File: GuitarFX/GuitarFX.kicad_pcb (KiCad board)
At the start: 4 copper layers, 70 x 85 mm, 122 parts, among them IC401 PCM3060PWR, J202 Screw_Terminal_01x02, J301 USB_C_Receptacle_USB2.0, J302 Conn_ARM_SWD_TagConnect_TC2030, J303 Screw_Terminal_01x06, J401 Screw_Terminal_01x02, J402 Screw_Terminal_01x02, SW301 SW_SPDT, U201 NCP718xSN500, U202 NCP1117-3.3_SOT223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

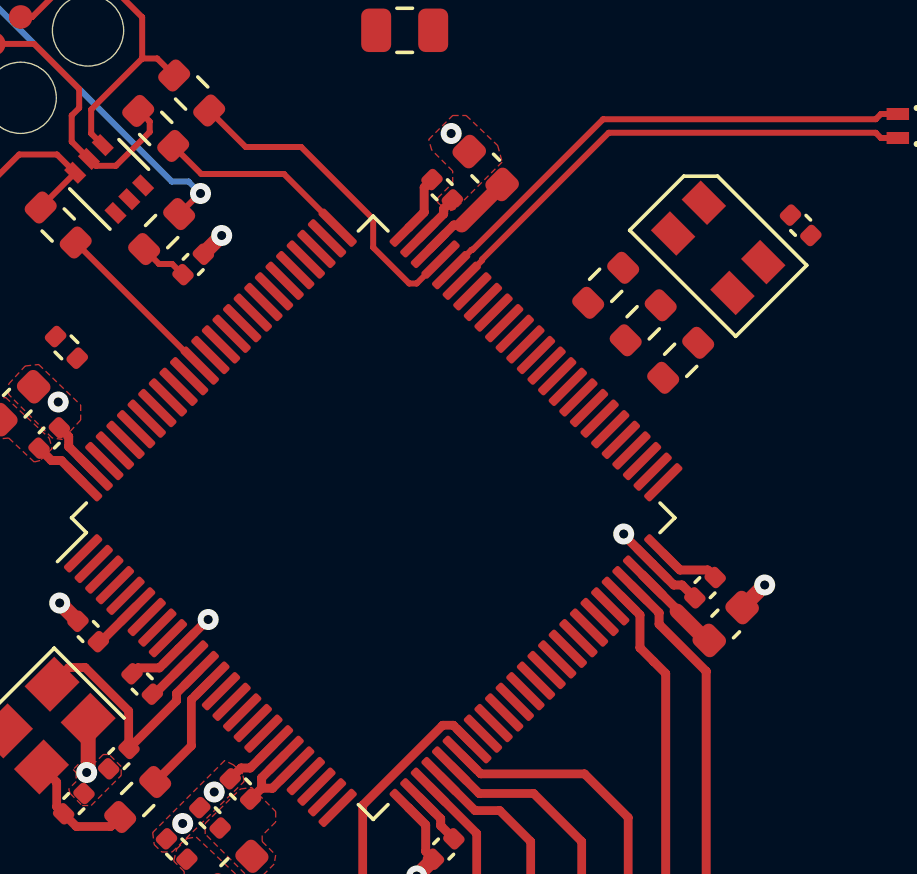
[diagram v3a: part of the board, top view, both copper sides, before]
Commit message: RGB led routing complete
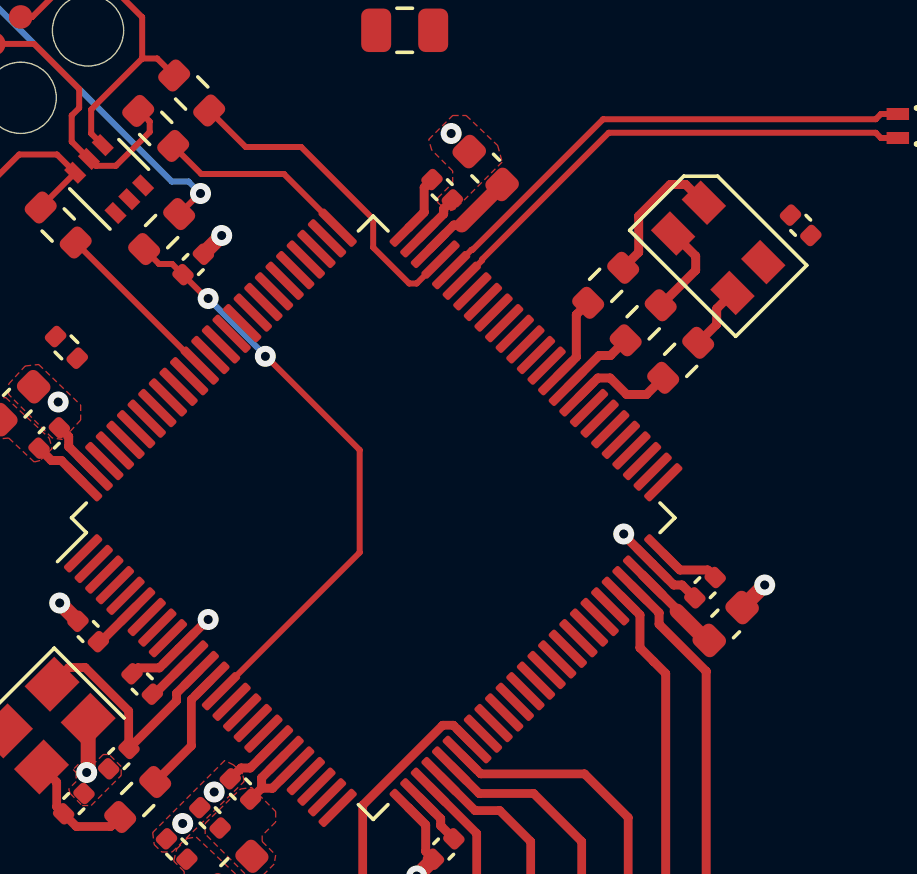
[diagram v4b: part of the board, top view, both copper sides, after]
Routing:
- net /MCU/MCU_NRST: track 1.65 -> 19.9 mm, vias 0 -> 2
- net /MCU/LED_R: track 0.00 -> 4.80 mm
- net /MCU/TIM4_CH1: track 0.00 -> 3.55 mm
- net /MCU/LED_G: track 0.00 -> 3.19 mm
- net /MCU/TIM4_CH3: track 0.00 -> 2.87 mm
- net /MCU/TIM4_CH2: track 0.00 -> 2.57 mm
- net /MCU/LED_B: track 0.00 -> 2.14 mm
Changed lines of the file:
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@@
   (segment (start 136.25 99.2) (end 135.105543 99.2) (width 0.29337) (layer "F.Cu") (net 11))
   (segment (start 137.863402 80.45) (end 137.36565 79.952248) (width 0.2) (layer "F.Cu") (net 12))
+  (segment (start 144.55 86.65) (end 144.55 90.067107) (width 0.2) (layer "F.Cu") (net 12))
   (segment (start 138.660589 80.805334) (end 138.655334 80.805334) (width 0.2) (layer "F.Cu") (net 12))
   (segment (start 138.655334 80.805334) (end 138.3 80.45) (width 0.2) (layer "F.Cu") (net 12))
+  (segment (start 141.405971 83.528532) (end 141.428532 83.528532) (width 0.2) (layer "F.Cu") (net 12))
+  (segment (start 141.428532 83.528532) (end 144.55 86.65) (width 0.2) (layer "F.Cu") (net 12))
+  (segment (start 139.5 81.6) (end 139.455255 81.6) (width 0.2) (layer "F.Cu") (net 12))
   (segment (start 138.3 80.45) (end 137.863402 80.45) (width 0.2) (layer "F.Cu") (net 12))
+  (segment (start 139.455255 81.6) (end 138.660589 80.805334) (width 0.2) (layer "F.Cu") (net 12))
+  (segment (start 144.55 90.067107) (end 139.926509 94.690598) (width 0.2) (layer "F.Cu") (net 12))
+  (via (at 139.5 81.6) (size 0.7) (drill 0.3) (layers "F.Cu" "B.Cu") (net 12))
+  (via (at 141.405971 83.528532) (size 0.7) (drill 0.3) (layers "F.Cu" "B.Cu") (net 12))
+  (segment (start 141.405971 83.528532) (end 141.405971 83.505971) (width 0.2) (layer "B.Cu") (net 12))
+  (segment (start 141.405971 83.505971) (end 139.5 81.6) (width 0.2) (layer "B.Cu") (net 12))
   (segment (start 153.962578 90.801511) (end 155.15 91.988933) (width 0.3) (layer "F.Cu") (net 13))
   (segment (start 155.15 91.988933) (end 155.15 92) (width 0.3) (layer "F.Cu") (net 13))
@@
   (segment (start 134.460889 76.8) (end 133.2 76.8) (width 0.2) (layer "F.Cu") (net 41))
   (segment (start 129.85 75.8) (end 129.85 74.888594) (width 0.2) (layer "F.Cu") (net 41))
+  (segment (start 155.415305 77.8) (end 154.9 77.8) (width 0.3) (layer "F.Cu") (net 42))
+  (segment (start 153.85 80.06) (end 153.333363 80.576637) (width 0.3) (layer "F.Cu") (net 42))
+  (segment (start 154.9 77.8) (end 153.85 78.85) (width 0.3) (layer "F.Cu") (net 42))
+  (segment (start 153.85 78.85) (end 153.85 80.06) (width 0.3) (layer "F.Cu") (net 42))
+  (segment (start 156.022703 78.407398) (end 155.415305 77.8) (width 0.3) (layer "F.Cu") (net 42))
+  (segment (start 155.75 80.185305) (end 155.75 80.66) (width 0.3) (layer "F.Cu") (net 43))
+  (segment (start 155.75 80.66) (end 154.583363 81.826637) (width 0.3) (layer "F.Cu") (net 43))
+  (segment (start 154.997398 79.432703) (end 155.75 80.185305) (width 0.3) (layer "F.Cu") (net 43))
+  (segment (start 156.45 81.939899) (end 156.45 82.46) (width 0.3) (layer "F.Cu") (net 44))
+  (segment (start 156.45 82.46) (end 155.833363 83.076637) (width 0.3) (layer "F.Cu") (net 44))
+  (segment (start 156.977297 81.412602) (end 156.45 81.939899) (width 0.3) (layer "F.Cu") (net 44))
   (segment (start 166.356249 76.8) (end 165.631249 76.075) (width 0.2) (layer "F.Cu") (net 45))
   (segment (start 164.900001 76.25) (end 164.3375 76.25) (width 0.2) (layer "F.Cu") (net 45))
@@
   (segment (start 139.219402 83.836509) (end 139.186509 83.836509) (width 0.2) (layer "F.Cu") (net 80))
   (segment (start 139.186509 83.836509) (end 135.083363 79.733363) (width 0.2) (layer "F.Cu") (net 80))
+  (segment (start 153.45 84.8) (end 154.11 84.8) (width 0.3) (layer "F.Cu") (net 81))
+  (segment (start 152.488427 84.25) (end 152.9 84.25) (width 0.3) (layer "F.Cu") (net 81))
+  (segment (start 151.841258 84.897169) (end 152.488427 84.25) (width 0.3) (layer "F.Cu") (net 81))
+  (segment (start 152.9 84.25) (end 153.45 84.8) (width 0.3) (layer "F.Cu") (net 81))
+  (segment (start 154.11 84.8) (end 154.666637 84.243363) (width 0.3) (layer "F.Cu") (net 81))
+  (segment (start 152.91 83.5) (end 153.416637 82.993363) (width 0.3) (layer "F.Cu") (net 82))
+  (segment (start 152.531321 83.5) (end 152.91 83.5) (width 0.3) (layer "F.Cu") (net 82))
+  (segment (start 151.487705 84.543616) (end 152.531321 83.5) (width 0.3) (layer "F.Cu") (net 82))
+  (segment (start 151.771283 83.55293) (end 151.771283 82.138717) (width 0.3) (layer "F.Cu") (net 83))
+  (segment (start 151.771283 82.138717) (end 152.166637 81.743363) (width 0.3) (layer "F.Cu") (net 83))
+  (segment (start 151.134151 84.190062) (end 151.771283 83.55293) (width 0.3) (layer "F.Cu") (net 83))
   (segment (start 152.045735 97.445735) (end 153.5 98.9) (width 0.29337) (layer "F.Cu") (net 85))
   (segment (start 153.5 98.9) (end 153.5 105.675) (width 0.29337) (layer "F.Cu") (net 85))

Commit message: Routing complete for ADC section
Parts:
- moved C405 21.6 mm to (142.3, 136.8), turned to 90 degrees
- moved R403 19.3 mm to (144.6, 139.2), turned to 180 degrees
- moved U401 16.9 mm to (145.7, 136.8), turned to 0 degrees
- moved R401 16.4 mm to (146.8, 139.2), turned to 180 degrees
- moved C402 12.8 mm to (148.5, 136.3), turned to -90 degrees
- moved C420 5.18 mm to (135.7, 133.2), turned to 0 degrees
- moved D401 0.72 mm to (170.3, 130.9)
- moved R301 0.51 mm to (135.2, 83.4)
- moved D403 0.47 mm to (119.5, 131.2)
- moved U403 0.46 mm to (156.8, 130.6)
- moved C404 0.46 mm to (157.6, 128.0)
- moved C408 0.44 mm to (166.8, 133.3)
- moved C406 0.39 mm to (164.0, 133.3)
- moved R402 0.39 mm to (162.0, 133.3)
- moved U402 0.39 mm to (163.3, 130.6)
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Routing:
- net Net-(SW301-B): track 0.00 -> 24.3 mm
- net /Codec/CODEC_VOUT: track 0.00 -> 16.1 mm
- net GND: track 44.7 -> 59.6 mm, vias 37 -> 51
- net /Codec/CODEC_VIN: track 0.00 -> 13.4 mm
- net /Codec/IN_AA_BUFF_OUT: track 0.00 -> 11.0 mm
- net /Codec/AUDIO_VIN: track 0.00 -> 9.97 mm
- net Net-(C401-Pad2): track 0.00 -> 8.04 mm
- net /Codec/AUDIO_VOUT: track 0.00 -> 6.00 mm
- net /Codec/IN_BUF_OUT: track 0.00 -> 5.97 mm
- net /Codec/IN_RF: track 0.00 -> 4.88 mm
- net /Codec/IN_AA_BUFF_IN: track 0.00 -> 4.77 mm
- net CODEC_NRST: track 0.00 -> 3.84 mm
- net Net-(C409-Pad1): track 0.00 -> 3.60 mm
- net +5VA: track 2.24 -> 5.40 mm
- net /Codec/IN_BUF_IN: track 0.00 -> 3.02 mm
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
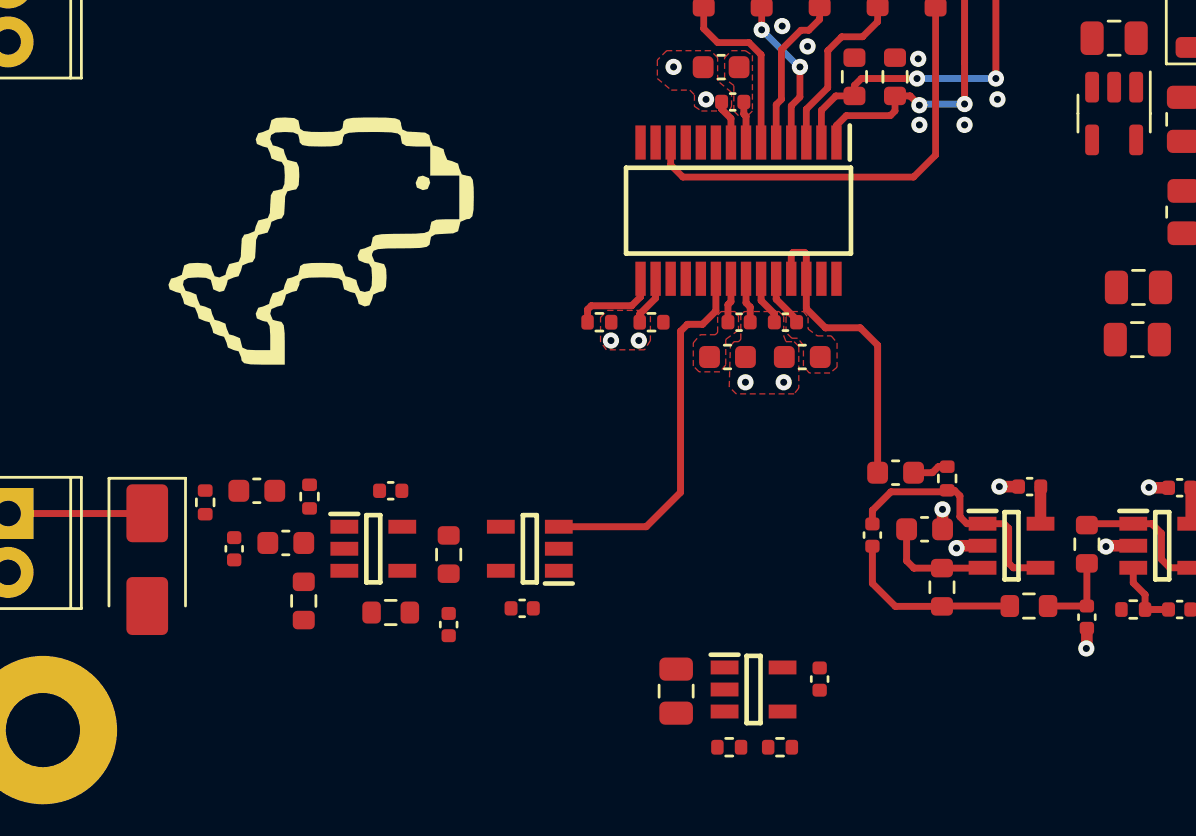
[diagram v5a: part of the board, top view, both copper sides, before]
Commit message: DAC portion routed
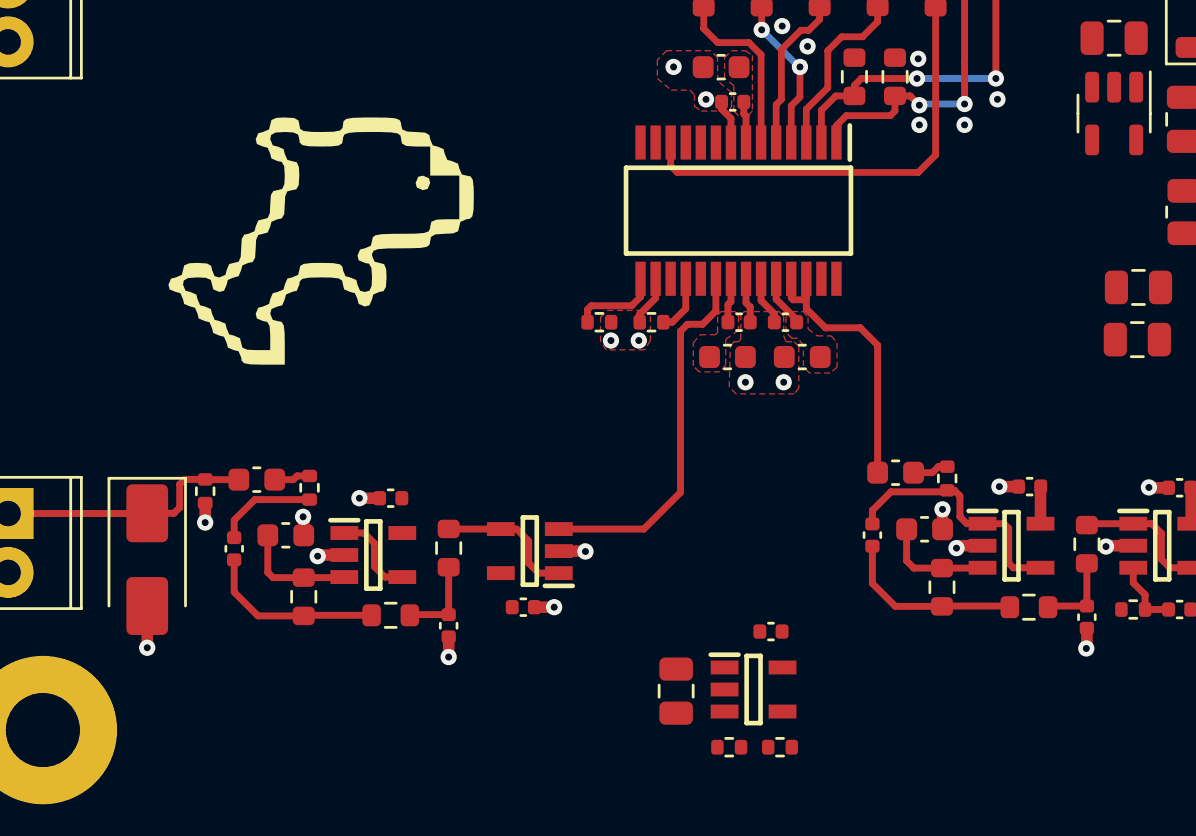
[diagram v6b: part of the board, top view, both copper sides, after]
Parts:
- moved C402 2.93 mm to (146.4, 134.2), turned to 180 degrees
- moved R427 0.48 mm to (122.0, 128.2)
- moved C422 0.48 mm to (124.2, 127.7)
- moved R425 0.38 mm to (126.5, 128.1)
- moved C424 0.33 mm to (125.5, 130.1)
- moved C421 0.32 mm to (130.0, 128.5)
- moved R421 0.28 mm to (132.5, 130.7)
- moved U407 0.27 mm to (129.2, 130.9)
- moved R423 0.18 mm to (126.2, 132.8)
- moved R422 0.12 mm to (130.0, 133.6)
- moved U406 0.10 mm to (136.0, 130.8)
- moved C420 0.07 mm to (135.7, 133.2)
- moved C423 0.05 mm to (132.5, 134.0)
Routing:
- net GND: track 59.6 -> 67.9 mm, vias 51 -> 59
- net /Codec/OUT_AA_BUFF_OUT: track 0.00 -> 8.24 mm
- net Net-(C419-Pad2): track 0.00 -> 7.75 mm
- net /Codec/OUT_BUF_OUT: track 0.00 -> 6.10 mm
- net /Codec/AUDIO_VOUT: track 6.00 -> 11.1 mm
- net /Codec/OUT_AA_BUFF_IN: track 0.00 -> 4.67 mm
- net Net-(C423-Pad1): track 0.00 -> 3.73 mm
- net Net-(IC401-VOUTR+): track 0.00 -> 2.50 mm
- net Net-(C422-Pad2): track 0.00 -> 1.57 mm
- net /Codec/CODEC_VIN: track 13.4 -> 12.1 mm

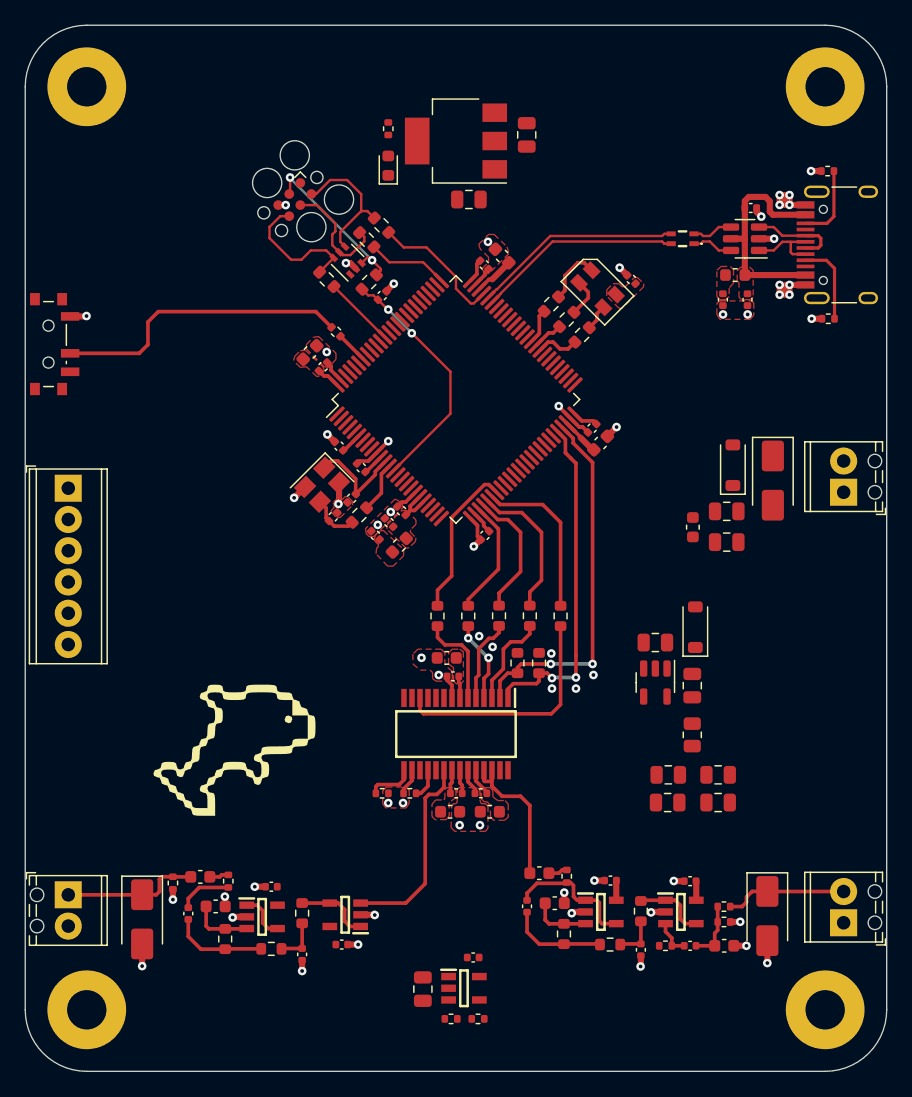
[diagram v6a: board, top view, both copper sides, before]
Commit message: Finished routing LDO sections
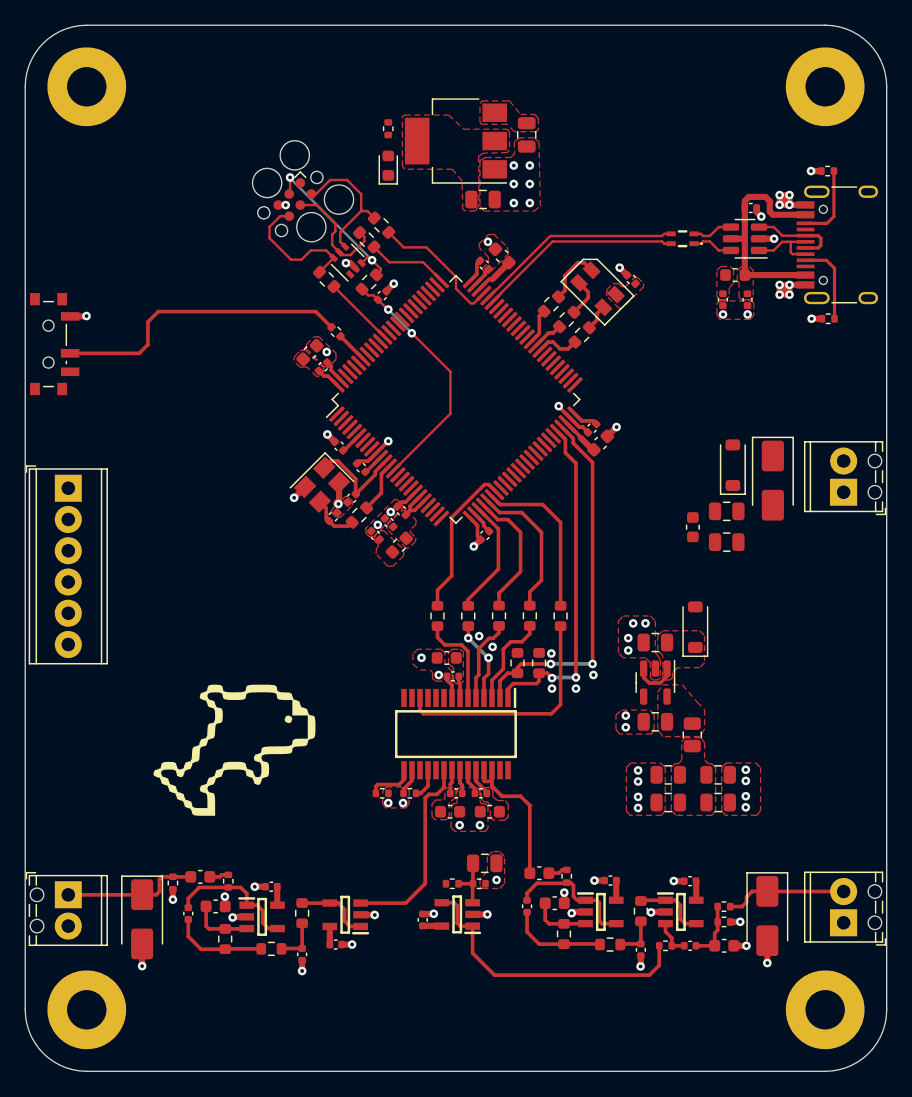
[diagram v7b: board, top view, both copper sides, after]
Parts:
- moved C405 11.4 mm to (147.3, 126.6), turned to 0 degrees
- moved R403 11.2 mm to (146.9, 128.3), turned to 0 degrees
- moved R401 11.2 mm to (144.7, 128.3), turned to 0 degrees
- moved U401 6.03 mm to (145.1, 130.8), turned to 180 degrees
- moved C402 5.11 mm to (142.3, 131.2), turned to 90 degrees
- moved C208 4.20 mm to (161.2, 115.1), turned to 180 degrees
- moved C209 1.15 mm to (147.2, 72.7)
- moved C420 0.49 mm to (135.2, 133.2)
- moved C203 0.05 mm to (162.2, 121.7)
- turned C207 to 180 degrees
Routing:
- net VCOM: track 0.00 -> 24.1 mm
- net +5VA: track 5.40 -> 9.94 mm
- net /Codec/VREF: track 0.00 -> 4.39 mm
- net /Power/VCC_FILT: track 0.00 -> 3.67 mm
- net /Codec/OUT_AA_BUFF_OUT: track 8.24 -> 10.9 mm
- net GND: track 67.9 -> 70.0 mm, vias 59 -> 82
- added copper zone on F.Cu, net +5V
- added copper zone on F.Cu, net /Power/VCC_FILT
